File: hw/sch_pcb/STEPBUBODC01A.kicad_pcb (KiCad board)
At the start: 2 copper layers, 40.1 x 30 mm, 18 parts, among them J1 HEADER_1x03, J2 HEADER_2x03_PARALLEL, J3 HEADER_1x03, J4 HEADER_1x03, J5 HEADER_2x03_PARALLEL, J6 HEADER_2x03_PARALLEL, U1 TPS631000DRLR

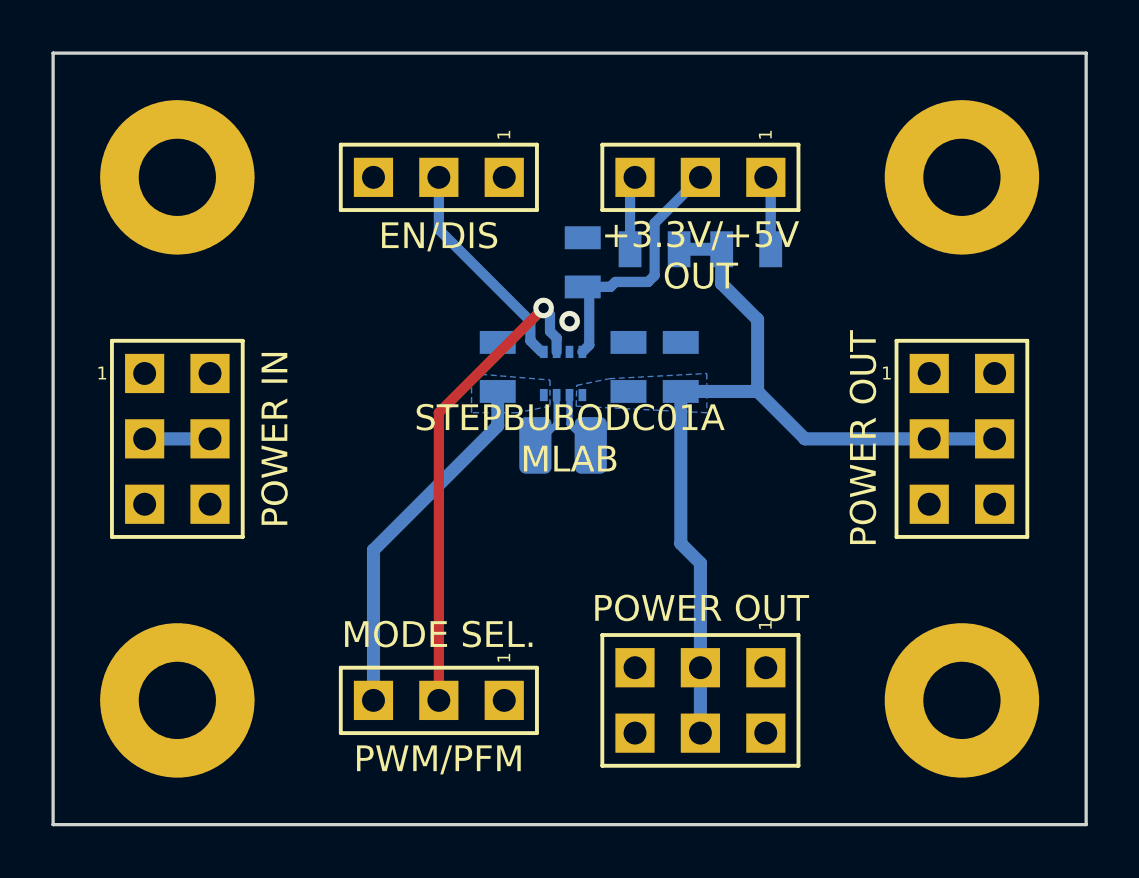
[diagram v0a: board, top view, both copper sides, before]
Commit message: silkscreen issues fixed
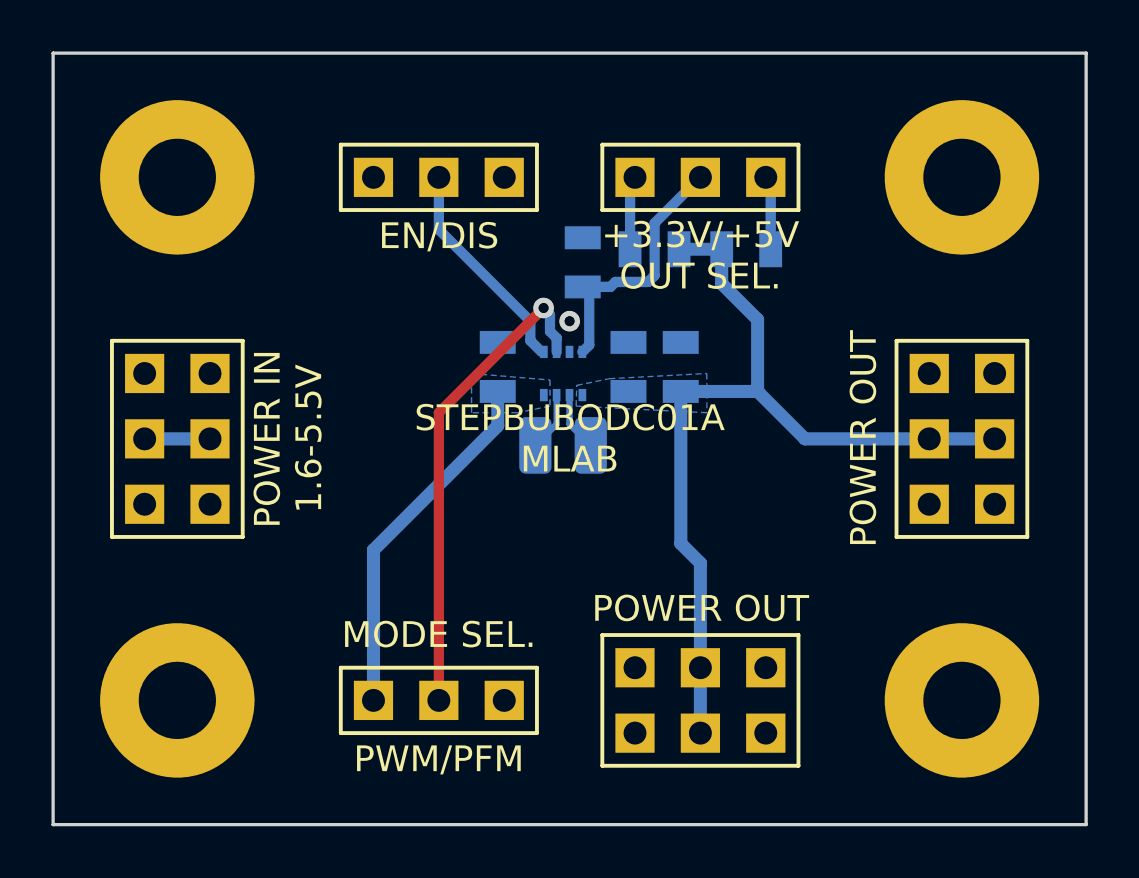
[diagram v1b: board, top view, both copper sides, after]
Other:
- board text added: "+3.3V/+5V OUT SEL."
- board text added: "POWER IN 1.6-5.5V"
- board text removed: "+3.3V/+5V OUT"
- board text removed: "POWER IN"
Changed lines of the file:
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@@
       (effects (font (size 1.5 1.5) (thickness 0.15)))
     )
-    (fp_text user "1" (at -1.651 -2.54 90) (layer "F.SilkS")
+    (fp_text user "1" (at -1.651 -2.54 90) (layer "F.SilkS") hide
       (effects (font (size 0.5 0.5) (thickness 0.05)))
     )
@@
       (effects (font (size 1.5 1.5) (thickness 0.15)))
     )
-    (fp_text user "1" (at -2.921 -2.54) (layer "F.SilkS")
+    (fp_text user "1" (at -2.921 -2.54) (layer "F.SilkS") hide
       (effects (font (size 0.5 0.5) (thickness 0.05)))
     )
@@
       (effects (font (size 1.5 1.5) (thickness 0.15)))
     )
-    (fp_text user "1" (at -1.651 -2.54 90) (layer "F.SilkS")
+    (fp_text user "1" (at -1.651 -2.54 90) (layer "F.SilkS") hide
       (effects (font (size 0.5 0.5) (thickness 0.05)))
     )
@@
       (effects (font (size 1.5 1.5) (thickness 0.15)))
     )
-    (fp_text user "1" (at -1.651 -2.54 90) (layer "F.SilkS")
+    (fp_text user "1" (at -1.651 -2.54 90) (layer "F.SilkS") hide
       (effects (font (size 0.5 0.5) (thickness 0.05)))
     )
@@
       (effects (font (size 1.5 1.5) (thickness 0.15)))
     )
-    (fp_text user "1" (at -2.921 -2.54 90) (layer "F.SilkS")
+    (fp_text user "1" (at -2.921 -2.54 90) (layer "F.SilkS") hide
       (effects (font (size 0.5 0.5) (thickness 0.05)))
     )
@@
       (effects (font (size 1.5 1.5) (thickness 0.15)))
     )
-    (fp_text user "1" (at -2.921 -2.54) (layer "F.SilkS")
+    (fp_text user "1" (at -2.921 -2.54) (layer "F.SilkS") hide
       (effects (font (size 0.5 0.5) (thickness 0.05)))
     )
@@
     (effects (font (size 1 1) (thickness 0.15)))
   )
-  (gr_text "+3.3V/+5V\nOUT" (at 147.32 79.248) (layer "F.SilkS")
+  (gr_text "+3.3V/+5V\nOUT SEL." (at 147.32 79.248) (layer "F.SilkS")
     (effects (font (size 1 1) (thickness 0.15)))
   )
@@
     (effects (font (size 1 1) (thickness 0.15)))
   )
-  (gr_text "POWER IN" (at 130.81 86.36 90) (layer "F.SilkS")
+  (gr_text "POWER IN\n1.6-5.5V" (at 131.318 86.36 90) (layer "F.SilkS")
     (effects (font (size 1 1) (thickness 0.15)))
   )

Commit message: pcb layout updated, ready for check
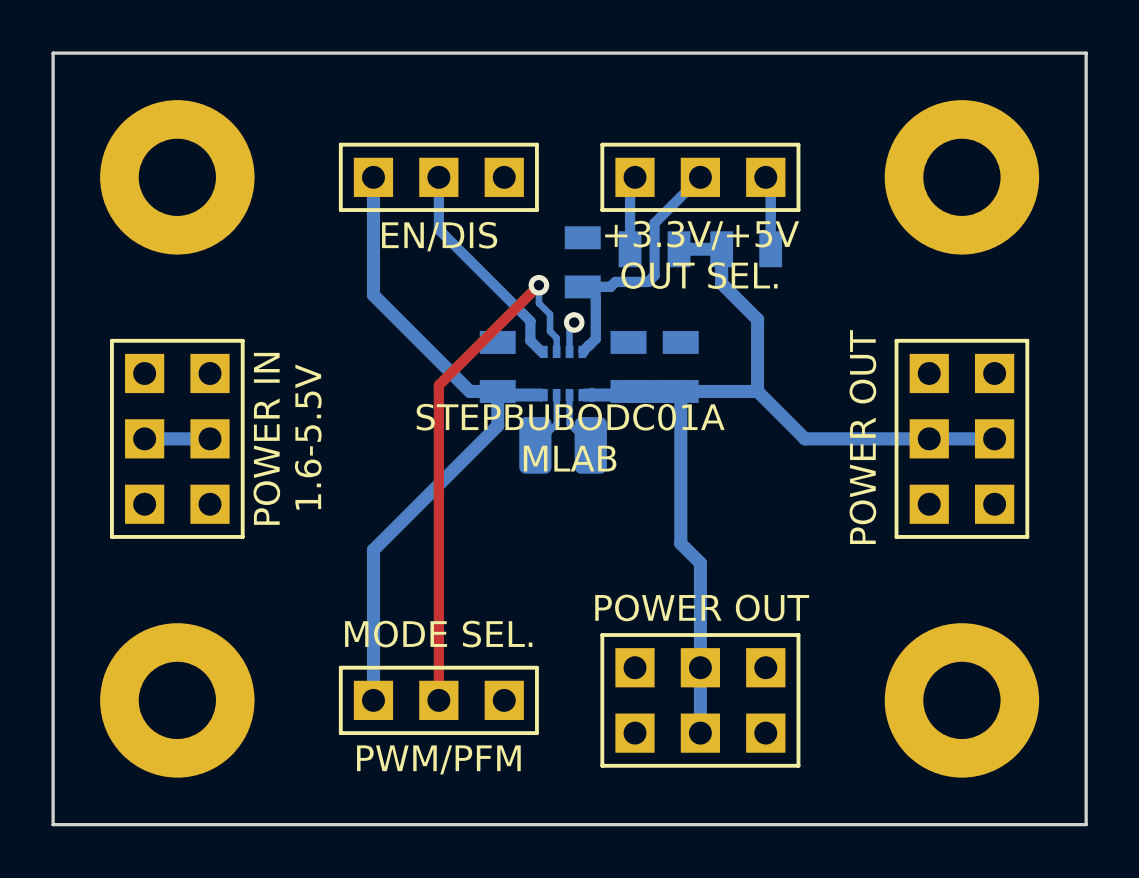
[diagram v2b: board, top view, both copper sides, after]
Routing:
- net /V_in: track 14.0 -> 26.7 mm
- net /V_out: track 34.5 -> 37.9 mm
- net /mod: track 18.8 -> 20.6 mm
- net GND: track 0.00 -> 1.22 mm, vias 0 -> 1
- net (no net): vias 1 -> 0
- added copper zone on B.Cu, net GND
- added copper zone on F.Cu, net GND
- removed copper zone on B.Cu, net /V_in
- removed copper zone on B.Cu, net /V_out
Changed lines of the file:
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@@
     (effects (font (size 1 1) (thickness 0.15)))
   )
-  (via (at 142.24 81.788) (size 0.8) (drill 0.4) (layers "F.Cu" "B.Cu") (free) (net 0))
+  (segment (start 139.5855 84.658) (end 139.446 84.5185) (width 0.25) (layer "B.Cu") (net 1))
+  (segment (start 139.5855 84.658) (end 141.132 84.658) (width 0.508) (layer "B.Cu") (net 1))
   (segment (start 139.446 85.852) (end 139.446 84.5185) (width 0.508) (layer "B.Cu") (net 1))
+  (segment (start 134.62 80.772) (end 134.62 76.2) (width 0.508) (layer "B.Cu") (net 1))
+  (segment (start 138.3665 84.5185) (end 134.62 80.772) (width 0.508) (layer "B.Cu") (net 1))
+  (segment (start 139.446 84.5185) (end 138.3665 84.5185) (width 0.508) (layer "B.Cu") (net 1))
   (segment (start 134.62 90.678) (end 139.446 85.852) (width 0.508) (layer "B.Cu") (net 1))
   (segment (start 134.62 96.52) (end 134.62 90.678) (width 0.508) (layer "B.Cu") (net 1))
+  (via (at 142.4178 81.8388) (size 0.8) (drill 0.4) (layers "F.Cu" "B.Cu") (free) (net 2))
+  (segment (start 142.236 82.0206) (end 142.4178 81.8388) (width 0.25) (layer "B.Cu") (net 2))
+  (segment (start 142.236 82.982) (end 142.236 82.0206) (width 0.25) (layer "B.Cu") (net 2))
   (segment (start 146.558 84.5185) (end 146.558 90.424) (width 0.508) (layer "B.Cu") (net 3))
   (segment (start 146.558 90.424) (end 147.32 91.186) (width 0.508) (layer "B.Cu") (net 3))
+  (segment (start 144.3865 84.658) (end 143.1038 84.658) (width 0.508) (layer "B.Cu") (net 3))
   (segment (start 156.21 86.36) (end 158.75 86.36) (width 0.508) (layer "B.Cu") (net 3))
-  (segment (start 144.3865 84.658) (end 144.526 84.5185) (width 0.25) (layer "B.Cu") (net 3))
+  (segment (start 143.1038 84.658) (end 143.1036 84.6582) (width 0.508) (layer "B.Cu") (net 3))
+  (segment (start 143.1036 84.6582) (end 143.1034 84.658) (width 0.508) (layer "B.Cu") (net 3))
   (segment (start 149.5425 84.5185) (end 149.5425 81.7245) (width 0.508) (layer "B.Cu") (net 3))
   (segment (start 147.32 91.186) (end 147.32 95.25) (width 0.508) (layer "B.Cu") (net 3))
@@
   (segment (start 149.5425 81.7245) (end 148.1455 80.3275) (width 0.508) (layer "B.Cu") (net 3))
   (segment (start 148.1455 78.994) (end 146.4945 78.994) (width 0.508) (layer "B.Cu") (net 3))
+  (segment (start 146.558 84.5185) (end 144.526 84.5185) (width 0.889) (layer "B.Cu") (net 3))
   (segment (start 147.32 95.25) (end 147.32 97.79) (width 0.508) (layer "B.Cu") (net 3))
+  (segment (start 143.1034 84.658) (end 142.84 84.658) (width 0.508) (layer "B.Cu") (net 3))
   (segment (start 151.384 86.36) (end 156.21 86.36) (width 0.508) (layer "B.Cu") (net 3))
   (segment (start 146.558 84.5185) (end 149.5425 84.5185) (width 0.508) (layer "B.Cu") (net 3))
@@
   (segment (start 141.148 82.982) (end 140.716 82.55) (width 0.4) (layer "B.Cu") (net 4))
   (segment (start 128.27 86.36) (end 125.73 86.36) (width 0.508) (layer "B.Cu") (net 5))
-  (segment (start 137.16 85.344) (end 141.228299 81.275701) (width 0.4) (layer "F.Cu") (net 6))
-  (segment (start 137.16 96.52) (end 137.16 85.344) (width 0.4) (layer "F.Cu") (net 6))
-  (via (at 141.228299 81.275701) (size 0.8) (drill 0.4) (layers "F.Cu" "B.Cu") (net 6))
-  (segment (start 141.736 82.4445) (end 141.736 82.982) (width 0.4) (layer "B.Cu") (net 6))
-  (segment (start 141.228299 81.275701) (end 141.478 81.525402) (width 0.25) (layer "B.Cu") (net 6))
-  (segment (start 141.478 81.525402) (end 141.478 82.1865) (width 0.4) (layer "B.Cu") (net 6))
-  (segment (start 141.478 82.1865) (end 141.736 82.4445) (width 0.4) (layer "B.Cu") (net 6))
+  (segment (start 137.16 84.2772) (end 137.16 96.52) (width 0.4) (layer "F.Cu") (net 6))
+  (segment (start 141.0462 80.391) (end 137.16 84.2772) (width 0.4) (layer "F.Cu") (net 6))
+  (via (at 141.0462 80.391) (size 0.8) (drill 0.4) (layers "F.Cu" "B.Cu") (net 6))
+  (segment (start 141.736 82.4445) (end 141.736 82.982) (width 0.254) (layer "B.Cu") (net 6))
+  (segment (start 141.0462 81.093602) (end 141.478 81.525402) (width 0.254) (layer "B.Cu") (net 6))
+  (segment (start 141.478 81.525402) (end 141.478 82.1865) (width 0.254) (layer "B.Cu") (net 6))
+  (segment (start 141.478 82.1865) (end 141.736 82.4445) (width 0.254) (layer "B.Cu") (net 6))
+  (segment (start 141.0462 80.391) (end 141.0462 81.093602) (width 0.254) (layer "B.Cu") (net 6))
   (segment (start 150.0505 76.3905) (end 149.86 76.2) (width 0.25) (layer "B.Cu") (net 7))
   (segment (start 150.0505 78.994) (end 150.0505 76.3905) (width 0.4) (layer "B.Cu") (net 7))
-  (segment (start 143.002 82.716) (end 142.736 82.982) (width 0.4) (layer "B.Cu") (net 8))
+  (segment (start 142.786 82.932) (end 142.786 82.982) (width 0.4) (layer "B.Cu") (net 8))
+  (segment (start 143.256 80.9625) (end 143.256 80.899) (width 0.4) (layer "B.Cu") (net 8))
+  (segment (start 143.002 82.716) (end 143.0138 82.716) (width 0.4) (layer "B.Cu") (net 8))
+  (segment (start 143.002 82.716) (end 142.786 82.932) (width 0.4) (layer "B.Cu") (net 8))
   (segment (start 142.748 80.4545) (end 143.002 80.7085) (width 0.25) (layer "B.Cu") (net 8))
   (segment (start 145.542 77.978) (end 145.542 80.01) (width 0.4) (layer "B.Cu") (net 8))
   (segment (start 145.288 80.264) (end 144.018 80.264) (width 0.4) (layer "B.Cu") (net 8))
+  (segment (start 143.256 82.4738) (end 143.256 80.9625) (width 0.4) (layer "B.Cu") (net 8))
   (segment (start 145.542 80.01) (end 145.288 80.264) (width 0.4) (layer "B.Cu") (net 8))
   (segment (start 144.018 80.264) (end 143.8275 80.4545) (width 0.4) (layer "B.Cu") (net 8))
-  (segment (start 143.002 80.7085) (end 143.002 82.716) (width 0.4) (layer "B.Cu") (net 8))
+  (segment (start 143.0138 82.716) (end 143.256 82.4738) (width 0.4) (layer "B.Cu") (net 8))
   (segment (start 143.8275 80.4545) (end 142.748 80.4545) (width 0.4) (layer "B.Cu") (net 8))
   (segment (start 147.32 76.2) (end 145.542 77.978) (width 0.4) (layer "B.Cu") (net 8))
@@
   (segment (start 142.236 85.789) (end 142.236 84.658) (width 0.25) (layer "B.Cu") (net 11))
   (segment (start 143.061 86.614) (end 142.236 85.789) (width 0.25) (layer "B.Cu") (net 11))
-  (zone (net 3) (net_name "/V_out") (layer "B.Cu") (hatch edge 0.508)
+  (zone (net 2) (net_name "GND") (layers F&B.Cu) (hatch edge 0.508)
     (connect_pads (clearance 0.254))
-    (min_thickness 0.127) (filled_areas_thickness no)
+    (min_thickness 0.254) (filled_areas_thickness no)
     (fill yes (thermal_gap 0.508) (thermal_bridge_width 0.508))
     (polygon
       (pts
-        (xy 147.573754 85.344)
-        (xy 142.494 85.09)
-        (xy 142.513546 84.282079)
-        (xy 143.778075 84.023077)
-        (xy 147.568625 83.819944)
+        (xy 162.306 101.346)
+        (xy 122.174 101.346)
+        (xy 122.174 71.374)
+        (xy 162.306 71.374)
       )
     )
-  )
-  (zone (net 1) (net_name "/V_in") (layer "B.Cu") (hatch edge 0.508)
-    (connect_pads (clearance 0.254))
-    (min_thickness 0.127) (filled_areas_thickness no)
-    (fill yes (thermal_gap 0.508) (thermal_bridge_width 0.508))
-    (polygon
-      (pts
-        (xy 141.478 84.074)
-        (xy 141.478 85.09)
-        (xy 140.208 85.344)
-        (xy 138.43 85.344)
-        (xy 138.43 83.82)
-      )
-    )
